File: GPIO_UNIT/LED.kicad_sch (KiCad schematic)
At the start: 13 parts, among them J901 Screw_Terminal_01x04, Q901 NPN_TOR, Q902 NPN_TOR, Q903 NPN_TOR

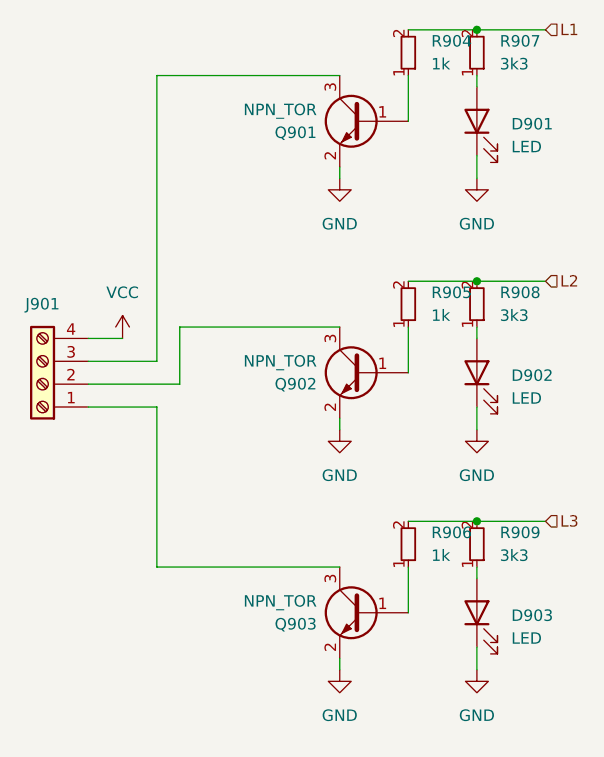
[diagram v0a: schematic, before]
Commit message: Digital pins are now able to use the analog pinnumbering as well. Pin can be set to an analog or digital pin number by simply pressing a or d respectively when editting the pinnumbers. Take note that one can fill in invalid analog pinnumbers. Also due to me support the arduino mega, I should remove pin number limit all togather.
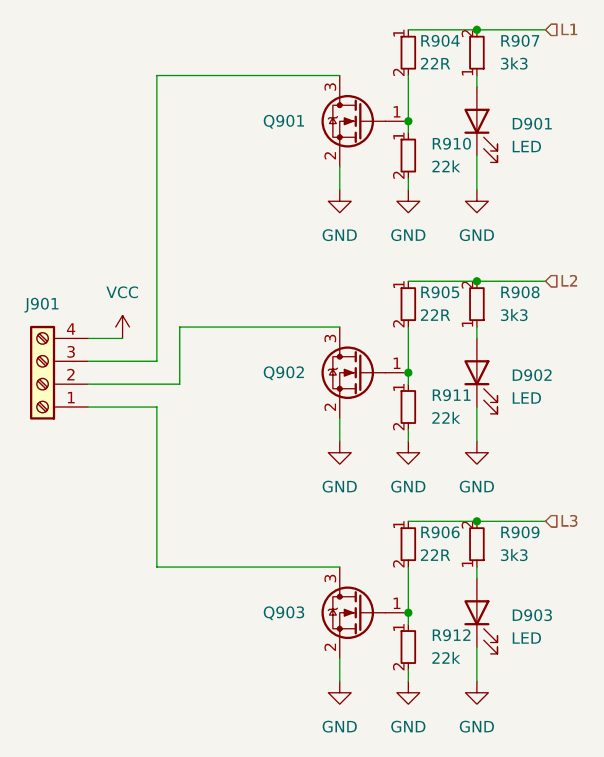
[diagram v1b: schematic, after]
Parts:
- removed Q901, Q902, Q903: NPN_TOR, Package_TO_SOT_SMD:SOT-23, symbol custom_kicad_lib_sk:NPN_TOR
- removed R904, R905, R906: 1k, custom_kicad_lib_sk:R_0603_smalltext, symbol resistors_0603:R_1k_0603
- added Q901, Q902, Q903: AO3400A, Package_TO_SOT_SMD:SOT-23, symbol custom_kicad_lib_sk:AO3400A
- added R904, R905, R906: 22R, custom_kicad_lib_sk:R_0603_smalltext, symbol resistors_0603:R_22R_0603
- added R910, R911, R912: 22k, custom_kicad_lib_sk:R_0603_smalltext, symbol resistors_0603:R_22k_0603
- J901: footprint TerminalBlock_Phoenix:TerminalBlock_Phoenix_MKDS-1,5-4-5.08_1x04_P5.08mm_Horizontal -> TerminalBlock_Phoenix:TerminalBlock_Phoenix_MPT-0,5-4-2.54_1x04_P2.54mm_Horizontal
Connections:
- net GND: now also Q901.2 (S), Q902.2 (S), Q903.2 (S), R910.2, R911.2, R912.2
- net L1: now also R904.1
- net L2: now also R905.1
- net L3: now also R906.1
- net at J901.1 (Pin_1): now also Q903.3 (D)
- net at J901.2 (Pin_2): now also Q902.3 (D)
- net at J901.3 (Pin_3): now also Q901.3 (D)
- new net: Q902.1 (G), R905.2, R911.1
- new net: Q901.1 (G), R904.2, R910.1
- new net: Q903.1 (G), R906.2, R912.1
